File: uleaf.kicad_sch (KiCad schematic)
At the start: 22 parts, among them J2 SWD Debug, J3 Conn_01x10, J4 Conn_01x10, U1 STM32G474CCUx, U2 PCM5102, U3 APS6404L-3SQRx-SN, U4 W25Q128JVS, Y1 Crystal_GND24

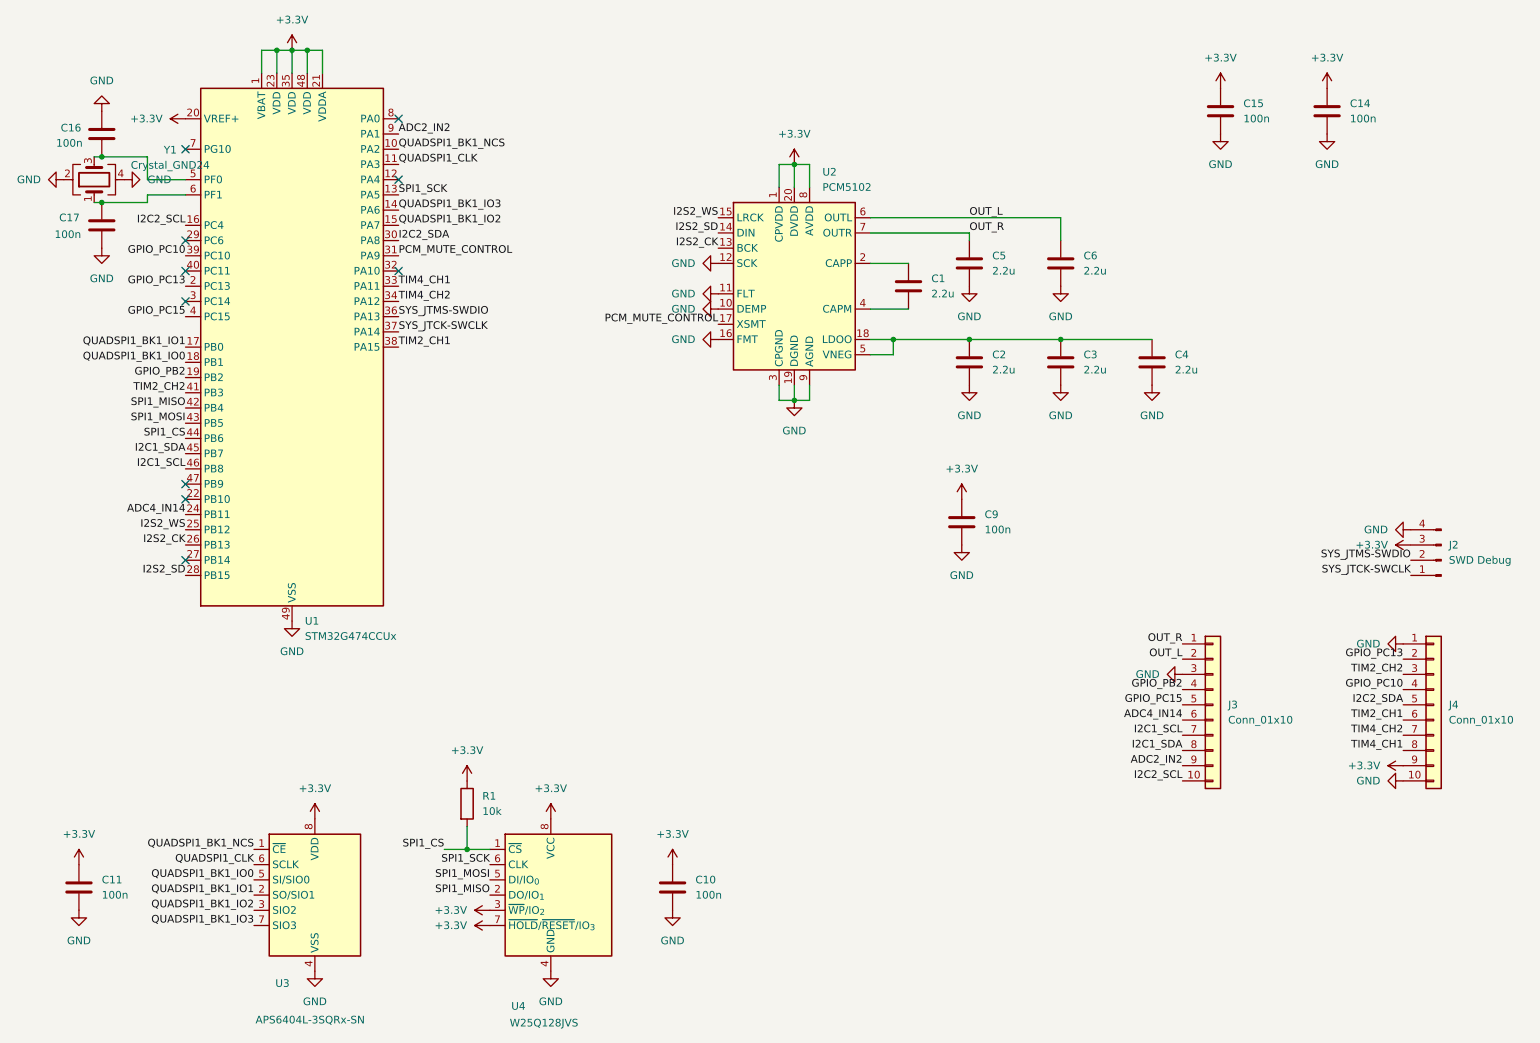
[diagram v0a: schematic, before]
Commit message: Fixed problem with VNEG pin
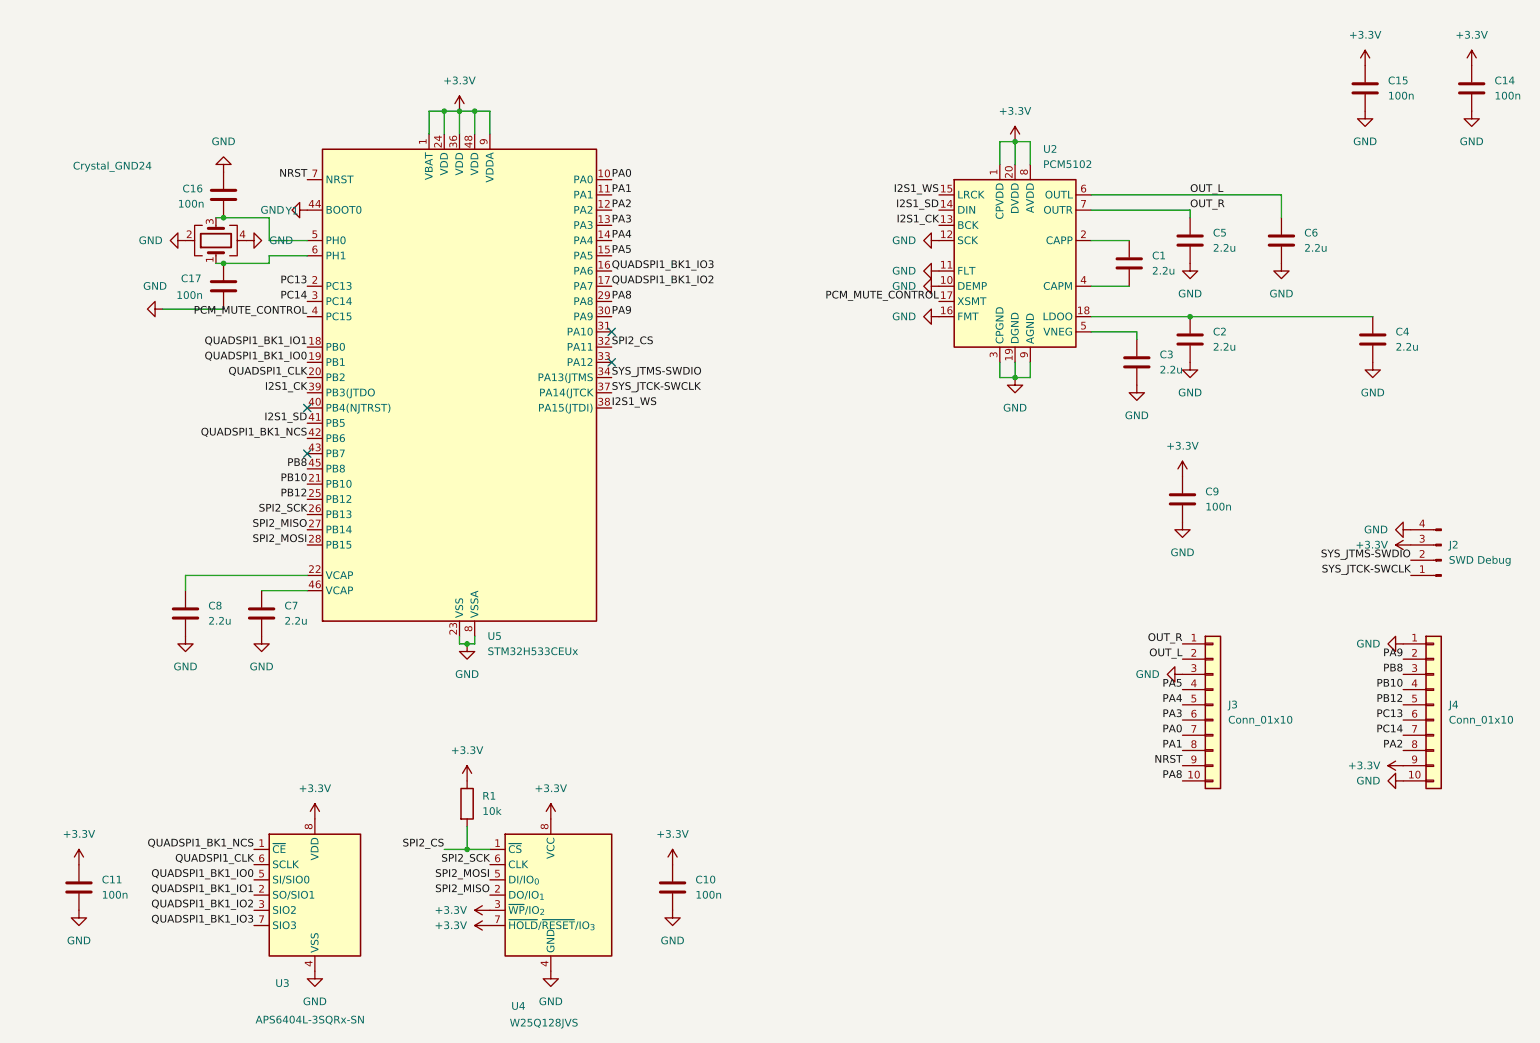
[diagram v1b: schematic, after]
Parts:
- removed U1: STM32G474CCUx, Package_DFN_QFN:QFN-48-1EP_7x7mm_P0.5mm_EP5.6x5.6mm, symbol MCU_ST_STM32G4:STM32G474CCUx
- added C7, C8: 2.2u, Capacitor_SMD:C_0603_1608Metric, symbol Device:C
- added U5: STM32H533CEUx, Package_DFN_QFN:QFN-48-1EP_7x7mm_P0.5mm_EP5.6x5.6mm, symbol MCU_ST_STM32H5:STM32H533CEUx
- J3, J4: footprint uleaf:PinHeader_1x10_P2.54mm_Vertical -> uleaf:PinHeader_1x10_P2.54mm_Vertical_Castellated
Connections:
- net +3.3V: now also U5.1 (VBAT), U5.24 (VDD), U5.36 (VDD), U5.48 (VDD), U5.9 (VDDA)
- net GND: now also C7.1, C8.1, U5.23 (VSS), U5.35 (VSS), U5.44 (BOOT0), U5.47 (VSS), U5.49 (VSS), U5.8 (VSSA)
- net PCM_MUTE_CONTROL: now also U5.4 (PC15)
- net QUADSPI1_BK1_IO0: now also U5.19 (PB1)
- net QUADSPI1_BK1_IO1: now also U5.18 (PB0)
- net QUADSPI1_BK1_IO2: now also U5.17 (PA7)
- net QUADSPI1_BK1_IO3: now also U5.16 (PA6)
- net QUADSPI1_BK1_NCS: now also U5.42 (PB6)
- net QUADSPI1_CLK: now also U5.20 (PB2)
- net SYS_JTCK-SWCLK: now also U5.37 (PA14(JTCK)
- net SYS_JTMS-SWDIO: now also U5.34 (PA13(JTMS)
- net at C17.2, Y1.1: now also U5.6 (PH1)
- net at C16.1, Y1.3: now also U5.5 (PH0)
- net at C2.2, C4.2, U2.18 (LDOO): no longer C3.2, U2.5 (VNEG)
- net ADC2_IN2 renamed NRST
- net NRST: now also U5.7 (NRST)
- net ADC4_IN14 renamed PA3
- net PA3: now also U5.13 (PA3)
- net GPIO_PB2 renamed PA5
- net PA5: now also U5.15 (PA5)
- net GPIO_PC10 renamed PB10
- net PB10: now also U5.21 (PB10)
- net GPIO_PC13 renamed PA9
- net PA9: now also U5.30 (PA9)
- net GPIO_PC15 renamed PA4
- net PA4: now also U5.14 (PA4)
- net I2C1_SCL renamed PA0
- net PA0: now also U5.10 (PA0)
- net I2C1_SDA renamed PA1
- net PA1: now also U5.11 (PA1)
- net I2C2_SCL renamed PA8
- net PA8: now also U5.29 (PA8)
- net I2C2_SDA renamed PB12
- net PB12: now also U5.25 (PB12)
- net I2S2_CK renamed I2S1_CK
- net I2S1_CK: now also U5.39 (PB3(JTDO)
- net I2S2_SD renamed I2S1_SD
- net I2S1_SD: now also U5.41 (PB5)
- net I2S2_WS renamed I2S1_WS
- net I2S1_WS: now also U5.38 (PA15(JTDI))
- net SPI1_CS renamed SPI2_CS
- net SPI2_CS: now also U5.32 (PA11)
- net SPI1_MISO renamed SPI2_MISO
- net SPI2_MISO: now also U5.27 (PB14)
- net SPI1_MOSI renamed SPI2_MOSI
- net SPI2_MOSI: now also U5.28 (PB15)
- net SPI1_SCK renamed SPI2_SCK
- net SPI2_SCK: now also U5.26 (PB13)
- net TIM2_CH1 renamed PC13
- net PC13: now also U5.2 (PC13)
- net TIM2_CH2 renamed PB8
- net PB8: now also U5.45 (PB8)
- net TIM4_CH1 renamed PA2
- net PA2: now also U5.12 (PA2)
- net TIM4_CH2 renamed PC14
- net PC14: now also U5.3 (PC14)
- new net: C8.2, U5.22 (VCAP)
- new net: C7.2, U5.46 (VCAP)
- new net: C3.2, U2.5 (VNEG)
- no-connect marks 10 -> 4
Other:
- moved on the sheet: C1, C14, C15, C16, C17, C2, C3, C4, C5, C6, C9, U2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

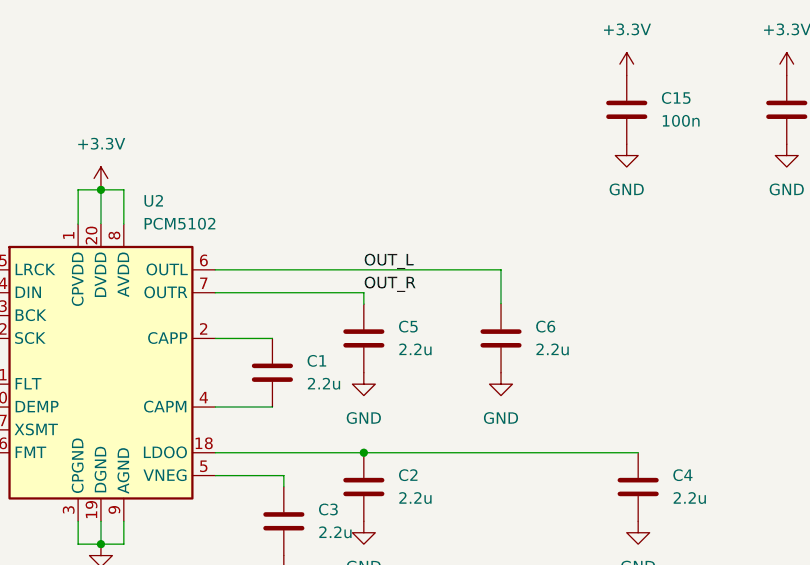
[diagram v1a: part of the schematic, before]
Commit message: Fixed problem with output DAC output filters
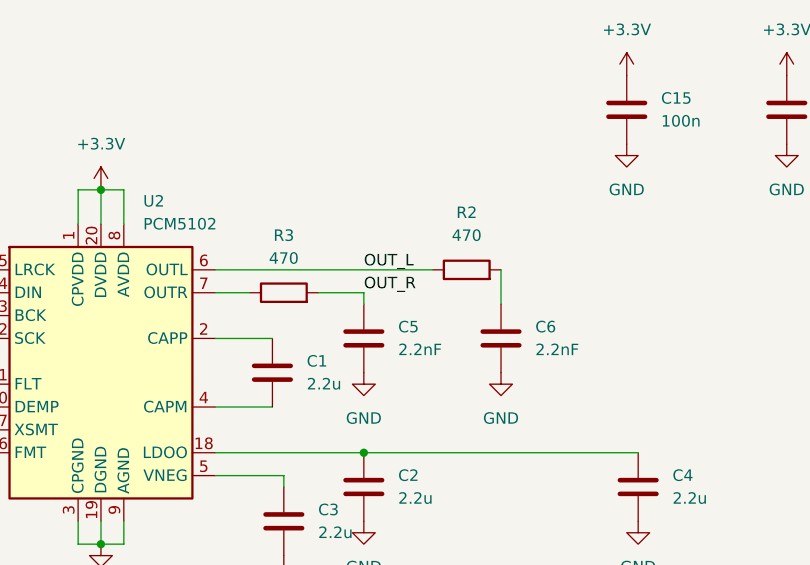
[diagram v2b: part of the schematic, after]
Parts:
- added R2, R3: 470, Resistor_SMD:R_0603_1608Metric, symbol Device:R
- C5, C6: value 2.2u -> 2.2nF
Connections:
- net OUT_L: now also R2.1; no longer C6.2
- net OUT_R: now also R3.2; no longer U2.7 (OUTR)
- new net: C6.2, R2.2
- new net: R3.1, U2.7 (OUTR)
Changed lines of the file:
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@@
 		(title "uLEAF Synth Core")
 		(date "2025-11-01")
-		(rev "0.2")
+		(rev "0.3")
 		(company "NU31 HackerSpace")
 		(comment 1 "Author: Artem Synytsyn <a.synytsyn@gmail.com>")

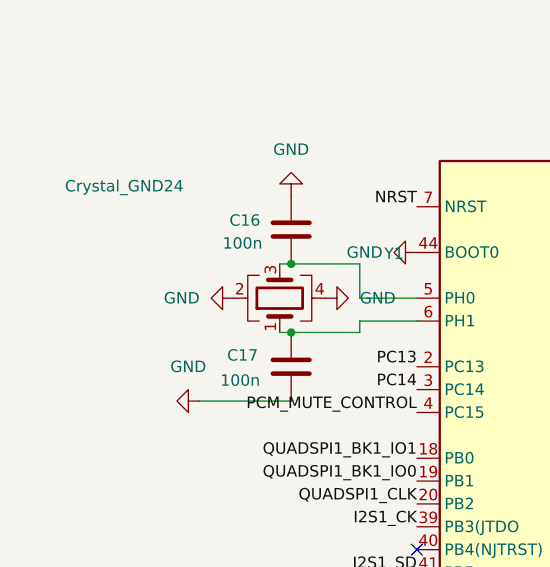
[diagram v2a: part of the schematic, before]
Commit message: Added values for crystal and caps
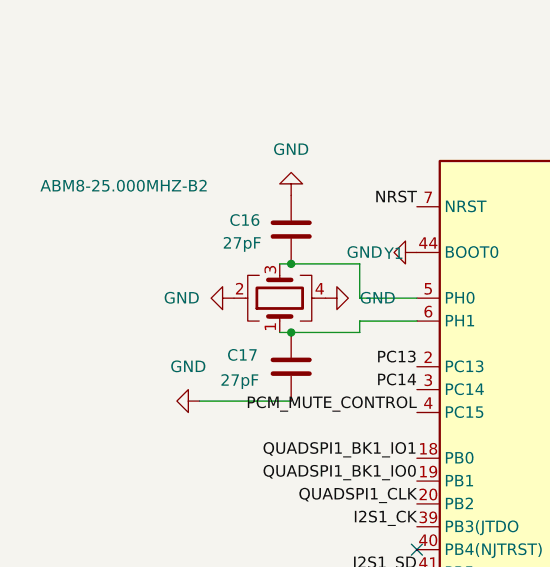
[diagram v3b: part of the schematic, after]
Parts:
- C16, C17: value 100n -> 27pF
- Y1: value Crystal_GND24 -> ABM8-25.000MHZ-B2

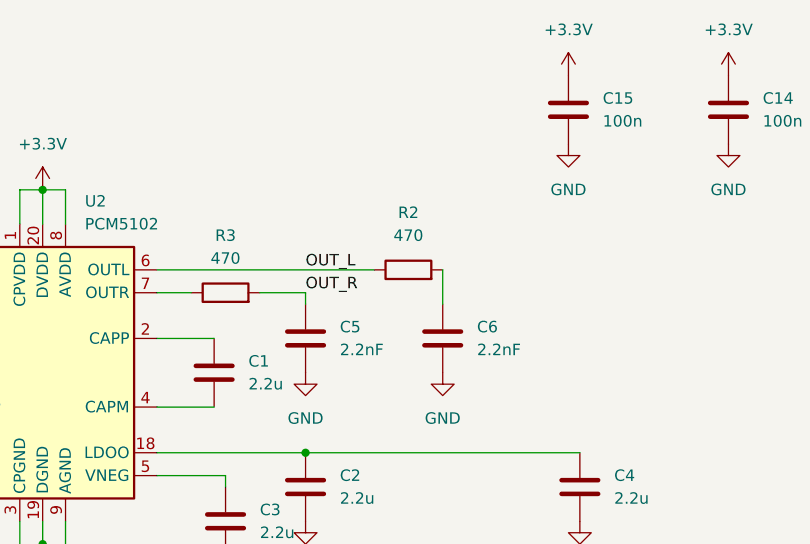
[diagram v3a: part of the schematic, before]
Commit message: Fixed problems with pcm connections, rev 0.4
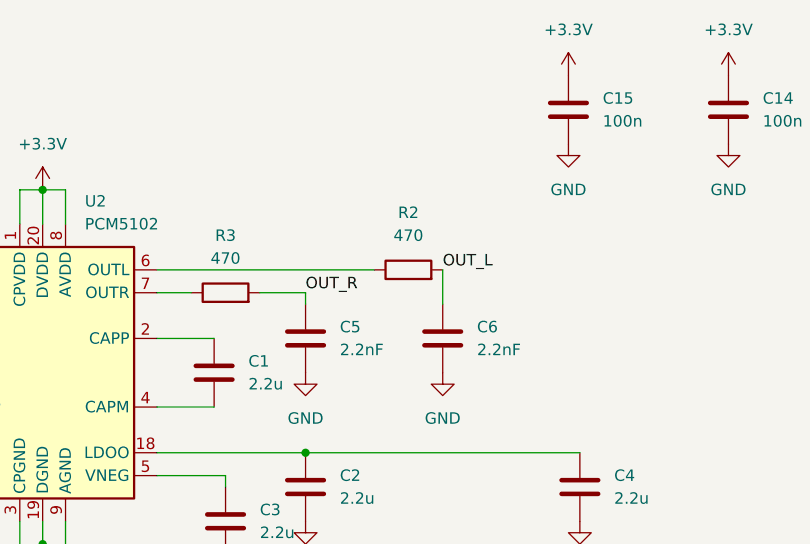
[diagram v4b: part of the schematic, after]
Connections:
- net OUT_L: now also C6.2, R2.2; no longer R2.1, U2.6 (OUTL)
- new net: R2.1, U2.6 (OUTL)
